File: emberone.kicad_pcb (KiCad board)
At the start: 6 copper layers, 125 x 125 mm, 468 parts, among them J1 Screw Terminal, J10 Conn_01x01, J11 Conn_01x01, J19 Conn_Coaxial, J2 Screw Terminal, J20 Conn_01x06, J3 Conn_01x01, J4 Conn_01x01, J5 Conn_01x01, J6 USB_C_Receptacle_USB2.0, J7 Conn_01x01, J8 Conn_01x01, J9 Conn_01x01, Q1 CSD18511Q5A, Q2 CSD18511Q5A, Q3 CSD18511Q5A, Q4 CSD18511Q5A, Q5 NVMFS5C645NLAFT1G, SW1 GT-TC029B-H025-L1N, SW2 GT-TC029B-H025-L1N, U1 LM25119PSQ/NOPB, U10 TLV1117LV33DCYR, U11 TPD1E05U06DYA, U12 TPD1E05U06DYA, U13 TMP451HQDQWRQ1, U2 DS4432U+, U27 RP2040, U28 MCP1824T-1202E/OT, U29 MCP1824T-1202E/OT, U3 INA260, U30 MCP1824T-1202E/OT, U32 MCP1824T-0802E, U4 SN74AVC4T774, U42 MCP1824T-0802E, U43 MCP1824T-0802E, U45 BM1362AC_MODE1, U46 BM1362AC_MODE0, U47 BM1362AC_MODE1, U48 MCP1824T-1202E/OT, U49 MCP1824T-1202E/OT, U5 25MHz, U50 MCP1824T-1202E/OT, U51 MCP1824T-0802E, U52 MCP1824T-0802E, U53 MCP1824T-0802E, U54 BM1362AC_MODE1, U55 BM1362AC_MODE0, U56 BM1362AC_MODE1, U57 MCP1824T-1202E/OT, U58 MCP1824T-1202E/OT, U59 MCP1824T-1202E/OT, U6 TMP1075, U60 MCP1824T-0802E, U61 MCP1824T-0802E, U62 MCP1824T-0802E, U63 BM1362AC_MODE1, U64 BM1362AC_MODE0, U65 BM1362AC_MODE1, U66 MCP1824T-1202E/OT, U67 MCP1824T-1202E/OT, U68 MCP1824T-1202E/OT, U69 MCP1824T-0802E, U7 AP74700Q, U70 MCP1824T-0802E, U71 MCP1824T-0802E, U72 BM1362AC_MODE1, U73 BM1362AC_MODE0, U74 BM1362AC_MODE1, U8 W25Q16JVUXIQ TR, U9 SK6812, Y1 12MHz

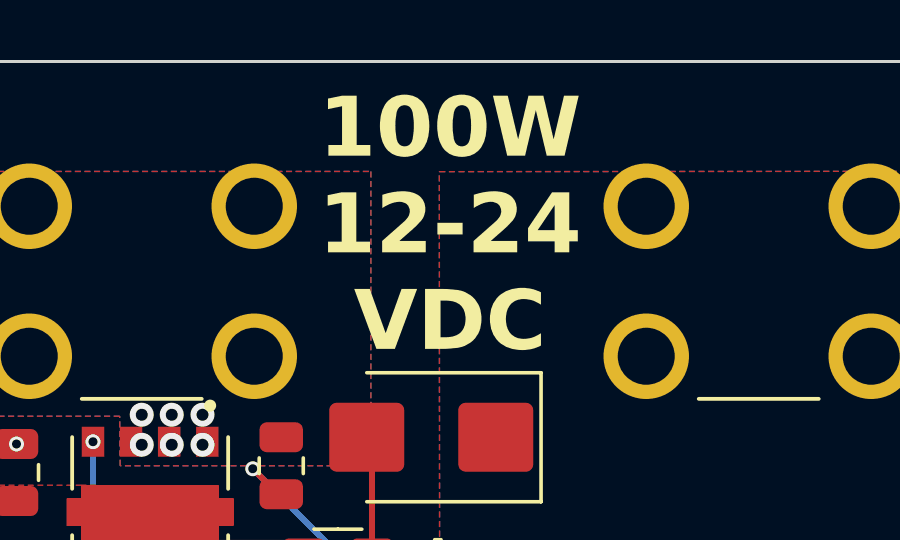
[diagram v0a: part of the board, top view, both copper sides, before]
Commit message: change input voltage silkscreen for #50
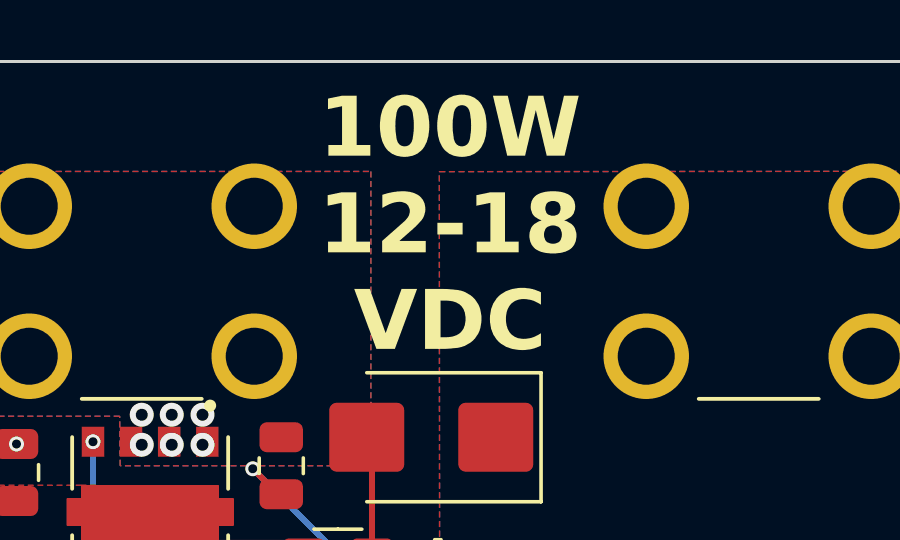
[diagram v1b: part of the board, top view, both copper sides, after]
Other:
- board text added: "100W 12-18 VDC"
- board text removed: "100W 12-24 VDC"
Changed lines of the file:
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@@
 		(layer "User.1")
 	)
-	(gr_text "100W\n12-24\nVDC"
+	(gr_text "100W\n12-18\nVDC"
 		(at 176.725 88.5 0)
 		(layer "F.SilkS")
